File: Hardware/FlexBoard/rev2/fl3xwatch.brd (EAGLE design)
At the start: 38.4 x 17.1 mm, 23 parts, among them J1 DISP

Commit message: Rev2.1 board
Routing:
- net +3V3: track 77.7 -> 76.6 mm
- net GND: vias 4 -> 5
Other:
- board size 38.4 x 17.1 mm -> 37.4 x 17.1 mm
- board text added: "Flexible"
- board text added: "Rigid"
- board text added: "rev2.1"
- board text removed: "rev2.0"
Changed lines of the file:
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@@
 <board>
 <plain>
-<wire x1="-0.3175" y1="0" x2="38.08" y2="0" width="0" layer="20"/>
-<wire x1="38.08" y1="0" x2="38.0746" y2="17.145" width="0" layer="20"/>
-<wire x1="38.0746" y1="17.145" x2="-0.3175" y2="17.145" width="0" layer="20"/>
+<wire x1="-0.3175" y1="0" x2="37.1275" y2="0" width="0" layer="20"/>
+<wire x1="37.1275" y1="0" x2="37.1221" y2="17.145" width="0" layer="20"/>
+<wire x1="37.1221" y1="17.145" x2="-0.3175" y2="17.145" width="0" layer="20"/>
 <wire x1="-0.3175" y1="17.145" x2="-0.3175" y2="0" width="0" layer="20"/>
 <text x="12.7" y="0.9525" size="1.016" layer="25">Designed In Thailand
 By TinLethax</text>
-<text x="30.48" y="1.5875" size="1.016" layer="1">rev2.0</text>
+<text x="30.48" y="1.5875" size="1.016" layer="1">rev2.1</text>
 <text x="21.2725" y="14.605" size="1.016" layer="25" font="vector">Fl3xWatchOLED</text>
+<wire x1="13.97" y1="16.51" x2="13.97" y2="13.0175" width="0.254" layer="25"/>
+<wire x1="13.97" y1="11.7475" x2="13.97" y2="3.81" width="0.254" layer="25"/>
+<wire x1="20.32" y1="16.51" x2="20.32" y2="1.905" width="0.254" layer="25"/>
+<wire x1="20.32" y1="0.635" x2="20.32" y2="0.3175" width="0.254" layer="25"/>
+<wire x1="13.97" y1="0.635" x2="13.97" y2="0.3175" width="0.254" layer="25"/>
+<wire x1="31.115" y1="16.51" x2="31.115" y2="15.875" width="0.254" layer="25"/>
+<wire x1="31.115" y1="14.2875" x2="31.115" y2="3.175" width="0.254" layer="25"/>
+<wire x1="31.115" y1="1.27" x2="31.115" y2="0.3175" width="0.254" layer="25"/>
+<text x="15.5575" y="4.445" size="1.27" layer="25" rot="R45">Flexible</text>
+<text x="33.3375" y="14.2875" size="0.6096" layer="25" rot="R45">Flexible</text>
+<text x="2.2225" y="13.6525" size="0.6096" layer="25" rot="R45">Rigid</text>
+<text x="27.94" y="1.27" size="0.6096" layer="25" rot="R45">Rigid</text>
 </plain>
 <attributes>
@@
 <attribute name="MOUSER_PART_NUMBER" value="798-FH35C11S03SHW50" x="2.8575" y="7.62" size="1.778" layer="27" rot="R270" display="off"/>
 <attribute name="MOUSER_PRICE-STOCK" value="https://www.mouser.com/Search/Refine.aspx?Keyword=798-FH35C11S03SHW50" x="2.8575" y="7.62" size="1.778" layer="27" rot="R270" display="off"/>
-<attribute name="NAME" x="2.8575" y="3.4925" size="1.27" layer="25" rot="R270" align="center"/>
+<attribute name="NAME" x="3.81" y="11.7475" size="1.27" layer="25" rot="R270" align="center"/>
 <attribute name="VALUE" x="2.8575" y="2.54" size="1.27" layer="27" align="center"/>
 </element>
@@
 <wire x1="12.507" y1="10.16" x2="11.7475" y2="9.4005" width="0.4064" layer="1"/>
 <wire x1="11.7475" y1="9.4005" x2="11.7475" y2="8.7655" width="0.4064" layer="1"/>
-<wire x1="1.905" y1="14.185" x2="4.1275" y2="14.185" width="0.254" layer="16"/>
+<wire x1="1.905" y1="14.185" x2="2.2225" y2="14.185" width="0.254" layer="16"/>
+<wire x1="2.2225" y1="14.185" x2="4.1275" y2="14.185" width="0.254" layer="16"/>
 <wire x1="4.1275" y1="14.185" x2="4.655" y2="14.7125" width="0.254" layer="16"/>
 <wire x1="4.655" y1="14.7125" x2="10.585" y2="14.7125" width="0.254" layer="16"/>
@@
 <wire x1="4.7275" y1="7.02" x2="4.7625" y2="6.985" width="0.1524" layer="1"/>
 <wire x1="0.9885" y1="9.12" x2="1.076" y2="9.2075" width="0.1524" layer="1"/>
-<wire x1="1.076" y1="9.2075" x2="2.2225" y2="9.2075" width="0.1524" layer="1"/>
-<via x="2.2225" y="9.2075" extent="1-16" drill="0.35"/>
-<wire x1="2.2225" y1="9.2075" x2="0.635" y2="10.795" width="0.1524" layer="16"/>
-<wire x1="0.635" y1="10.795" x2="0.635" y2="13.335" width="0.1524" layer="16"/>
-<wire x1="0.635" y1="13.335" x2="1.485" y2="14.185" width="0.1524" layer="16"/>
 <wire x1="1.485" y1="14.185" x2="1.905" y2="14.185" width="0.1524" layer="16"/>
-<wire x1="2.2225" y1="9.2075" x2="0.9525" y2="9.2075" width="0.1524" layer="16"/>
 <wire x1="0.9525" y1="9.2075" x2="0.9525" y2="6.985" width="0.1524" layer="16"/>
 <wire x1="0.9525" y1="6.985" x2="4.7625" y2="6.985" width="0.1524" layer="16"/>
@@
 <wire x1="6.0325" y1="6.77" x2="9.31" y2="6.77" width="0.1524" layer="16"/>
 <wire x1="9.31" y1="6.77" x2="12.7" y2="10.16" width="0.1524" layer="16"/>
+<wire x1="0.9885" y1="9.12" x2="0.901" y2="9.2075" width="0.1524" layer="1"/>
+<wire x1="0.901" y1="9.2075" x2="0.3175" y2="9.2075" width="0.1524" layer="1"/>
+<wire x1="0.3175" y1="13.6525" x2="0.635" y2="13.97" width="0.1524" layer="1"/>
+<wire x1="0.3175" y1="13.6525" x2="0.3175" y2="9.2075" width="0.1524" layer="1"/>
+<via x="0.635" y="13.97" extent="1-16" drill="0.35"/>
+<wire x1="0.635" y1="13.97" x2="2.0075" y2="13.97" width="0.1524" layer="16"/>
+<wire x1="2.0075" y1="13.97" x2="2.2225" y2="14.185" width="0.1524" layer="16"/>
 </signal>
 <signal name="GND">
@@
 <polygon width="0.1524" layer="1">
 <vertex x="-0.3175" y="17.145"/>
-<vertex x="38.1" y="17.145"/>
-<vertex x="38.1" y="0"/>
+<vertex x="37.1475" y="17.145"/>
+<vertex x="37.1475" y="0"/>
 <vertex x="-0.3175" y="0"/>
 </polygon>
 <polygon width="0.1524" layer="16">
-<vertex x="-0.3175" y="16.8275"/>
+<vertex x="-0.3175" y="0"/>
 <vertex x="-0.3175" y="17.145"/>
-<vertex x="37.7825" y="17.145"/>
-<vertex x="38.1" y="17.145"/>
-<vertex x="38.1" y="0"/>
-<vertex x="-0.3175" y="0"/>
+<vertex x="37.1475" y="17.145"/>
+<vertex x="37.1475" y="0"/>
 </polygon>
 <wire x1="7.0875" y1="8.5725" x2="7.2799" y2="8.5725" width="0.4064" layer="1"/>
@@
 <via x="10.93490625" y="10.16" extent="1-16" drill="0.35"/>
 <wire x1="9.74" y1="8.47" x2="10.4775" y2="9.2075" width="0.254" layer="16"/>
+<via x="11.7475" y="6.6675" extent="1-16" drill="0.35"/>
 </signal>
 <signal name="N$1">
@@
 <contactref element="R4" pad="2"/>
 <contactref element="R5" pad="2"/>
-<wire x1="8.1525" y1="4.7625" x2="7.835" y2="4.7625" width="0.1524" layer="1"/>
-<wire x1="6.4875" y1="6.1675" x2="6.4875" y2="6.11" width="0.1524" layer="1"/>
-<wire x1="7.835" y1="4.7625" x2="6.4875" y2="6.11" width="0.1524" layer="1"/>
-<wire x1="7.5725" y1="2.8575" x2="8.1525" y2="3.4375" width="0.1524" layer="1"/>
-<wire x1="8.1525" y1="4.7625" x2="8.1525" y2="3.4375" width="0.1524" layer="1"/>
-<wire x1="7.5725" y1="2.8575" x2="6.35" y2="2.8575" width="0.1524" layer="1"/>
 <via x="6.35" y="2.8575" extent="1-16" drill="0.35"/>
 <wire x1="6.35" y1="2.8575" x2="7.5725" y2="2.8575" width="0.1524" layer="16"/>
+<wire x1="8.1525" y1="4.7625" x2="8.1525" y2="3.4375" width="0.254" layer="1"/>
+<wire x1="8.1525" y1="3.4375" x2="7.5725" y2="2.8575" width="0.254" layer="1"/>
+<wire x1="6.35" y1="2.8575" x2="7.5725" y2="2.8575" width="0.254" layer="1"/>
+<wire x1="6.4875" y1="6.1675" x2="7.8925" y2="4.7625" width="0.254" layer="1"/>
+<wire x1="7.8925" y1="4.7625" x2="8.1525" y2="4.7625" width="0.254" layer="1"/>
 </signal>
 <signal name="SW">
@@
 <contactref element="U$1" pad="PC1"/>
 <wire x1="6.5375" y1="11.935" x2="6.9375" y2="11.935" width="0.1524" layer="1"/>
-<wire x1="2.2225" y1="11.43" x2="2.8575" y2="11.43" width="0.1524" layer="16"/>
-<wire x1="2.8575" y1="11.43" x2="6.0325" y2="11.43" width="0.1524" layer="16"/>
+<wire x1="2.2225" y1="11.43" x2="6.0325" y2="11.43" width="0.1524" layer="16"/>
 <via x="6.0325" y="11.43" extent="1-16" drill="0.35"/>
 <wire x1="6.0325" y1="11.43" x2="6.5375" y2="11.935" width="0.1524" layer="1"/>
@@
 <wire x1="1.006" y1="7.9375" x2="1.905" y2="7.9375" width="0.1524" layer="1"/>
 <via x="1.905" y="7.9375" extent="1-16" drill="0.35"/>
-<wire x1="2.8575" y1="8.5725" x2="2.2225" y2="7.9375" width="0.1524" layer="16"/>
 <wire x1="1.905" y1="7.9375" x2="2.2225" y2="7.9375" width="0.1524" layer="16"/>
-<wire x1="2.8575" y1="8.5725" x2="2.8575" y2="11.43" width="0.1524" layer="16"/>
+<wire x1="2.2225" y1="7.9375" x2="2.2225" y2="11.43" width="0.1524" layer="16"/>
 <wire x1="1.905" y1="12.485" x2="2.2225" y2="12.1675" width="0.1524" layer="16"/>
 <wire x1="2.2225" y1="12.1675" x2="2.2225" y2="11.43" width="0.1524" layer="16"/>
@@
 <wire x1="23.366371875" y1="5.903871875" x2="23.36636875" y2="5.90386875" width="0" layer="19" extent="1-1"/>
 </signal>
-<signal name="N$3">
-<via x="21.9075" y="13.6525" extent="1-16" drill="0.35"/>
-</signal>
-<signal name="N$4">
-<via x="14.605" y="9.2075" extent="1-16" drill="0.35"/>
-</signal>
-<signal name="N$6">
-<via x="16.8275" y="7.9375" extent="1-16" drill="0.35"/>
-</signal>
-<signal name="N$8">
-<via x="14.605" y="5.715" extent="1-16" drill="0.35"/>
-</signal>
-<signal name="N$9">
-<via x="16.8275" y="4.7625" extent="1-16" drill="0.35"/>
-</signal>
-<signal name="N$10">
-<via x="34.925" y="14.605" extent="1-16" drill="0.35"/>
-</signal>
-<signal name="N$11">
-<via x="30.48" y="13.335" extent="1-16" drill="0.35"/>
-</signal>
-<signal name="N$12">
-<via x="31.4325" y="5.3975" extent="1-16" drill="0.35"/>
-</signal>
-<signal name="N$13">
-<via x="26.3525" y="1.5875" extent="1-16" drill="0.35"/>
-</signal>
-<signal name="N$14">
-<via x="21.9075" y="1.5875" extent="1-16" drill="0.35"/>
-</signal>
-<signal name="N$15">
-<via x="35.8775" y="4.1275" extent="1-16" drill="0.35"/>
-</signal>
-<signal name="N$16">
-<via x="20.0025" y="15.24" extent="1-16" drill="0.35"/>
-</signal>
 </signals>

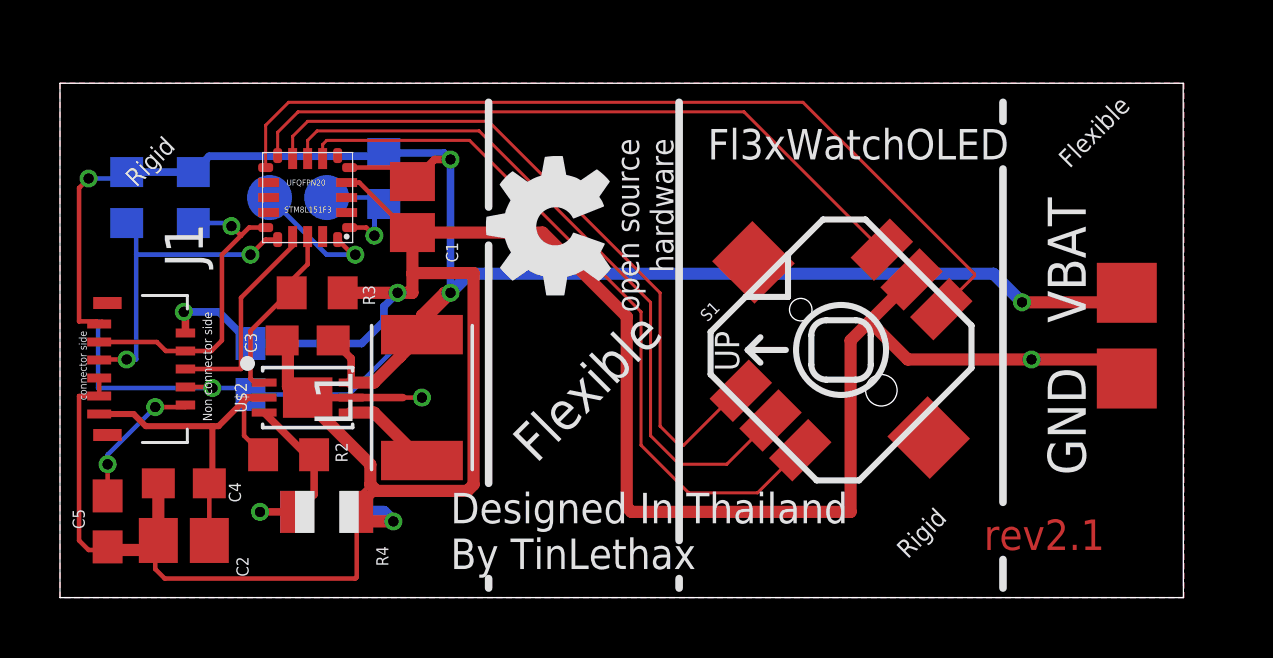
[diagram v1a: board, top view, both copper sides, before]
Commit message: added Rev 2.2 PCB
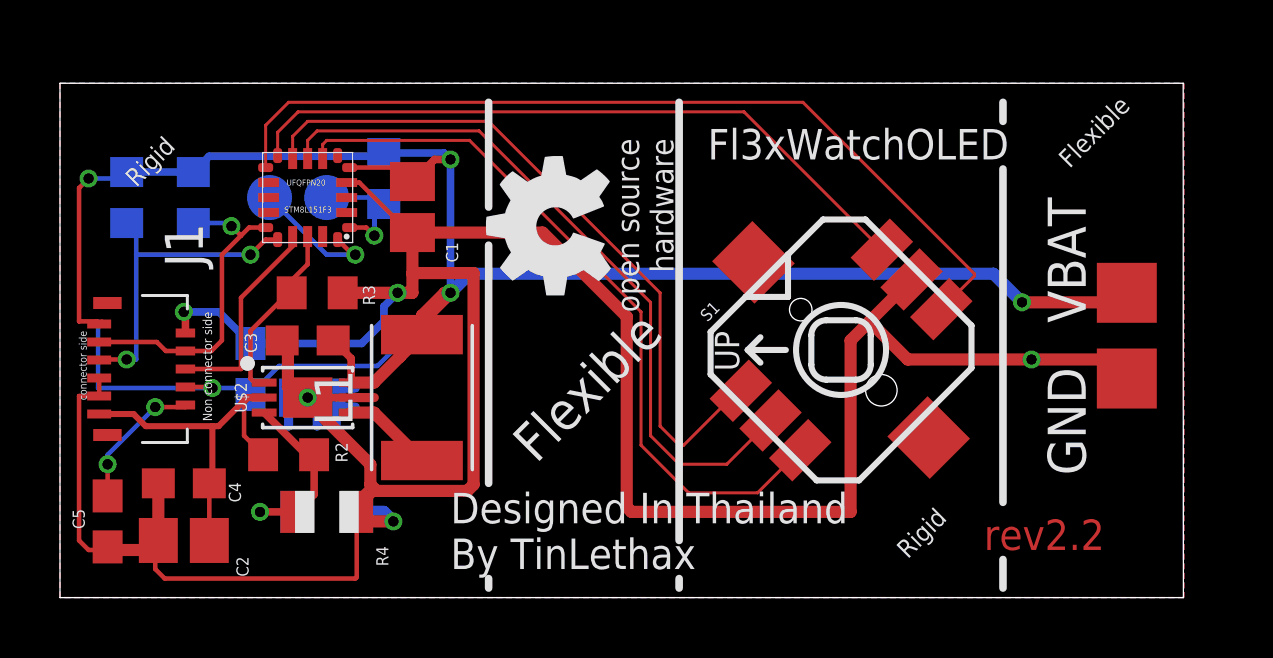
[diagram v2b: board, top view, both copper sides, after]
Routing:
- net GND: track 110.8 -> 108.6 mm
- net N$5: track 0.00 -> 0.63 mm
- net N$4: track 0.00 -> 0.63 mm
- net N$3: track 0.00 -> 0.63 mm
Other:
- board text added: "rev2.2"
- board text removed: "rev2.1"
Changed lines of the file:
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@@
 <drawing>
 <settings>
-<setting alwaysvectorfont="yes"/>
+<setting alwaysvectorfont="no"/>
 <setting verticaltext="up"/>
 </settings>
@@
 <text x="12.7" y="0.9525" size="1.016" layer="25">Designed In Thailand
 By TinLethax</text>
-<text x="30.48" y="1.5875" size="1.016" layer="1">rev2.1</text>
+<text x="30.48" y="1.5875" size="1.016" layer="1">rev2.2</text>
 <text x="21.2725" y="14.605" size="1.016" layer="25" font="vector">Fl3xWatchOLED</text>
 <wire x1="13.97" y1="16.51" x2="13.97" y2="13.0175" width="0.254" layer="25"/>
@@
 <text x="2.2225" y="13.6525" size="0.6096" layer="25" rot="R45">Rigid</text>
 <text x="27.94" y="1.27" size="0.6096" layer="25" rot="R45">Rigid</text>
+<rectangle x1="6.985" y1="6.0325" x2="9.2075" y2="7.3025" layer="16"/>
 </plain>
 <attributes>
@@
 <classes>
 <class number="0" name="default" width="0" drill="0">
+</class>
+<class number="1" name="Ground" width="0" drill="0">
 </class>
 </classes>
@@
 <wire x1="12.485" y1="14.82" x2="12.7" y2="14.605" width="0.254" layer="16"/>
 <wire x1="12.7" y1="14.605" x2="12.7" y2="10.16" width="0.254" layer="16"/>
-<wire x1="6.0325" y1="6.77" x2="9.31" y2="6.77" width="0.1524" layer="16"/>
-<wire x1="9.31" y1="6.77" x2="12.7" y2="10.16" width="0.1524" layer="16"/>
+<wire x1="6.0325" y1="6.77" x2="6.985" y2="7.7225" width="0.1524" layer="16"/>
+<wire x1="10.2625" y1="7.7225" x2="6.985" y2="7.7225" width="0.1524" layer="16"/>
+<wire x1="10.2625" y1="7.7225" x2="12.7" y2="10.16" width="0.1524" layer="16"/>
 <wire x1="0.9885" y1="9.12" x2="0.901" y2="9.2075" width="0.1524" layer="1"/>
 <wire x1="0.901" y1="9.2075" x2="0.3175" y2="9.2075" width="0.1524" layer="1"/>
@@
 <contactref element="GND" pad="TP"/>
 <contactref element="S1" pad="GND"/>
-<wire x1="7.9375" y1="6.6675" x2="9.3875" y2="6.6675" width="0.254" layer="1"/>
+<wire x1="7.9375" y1="6.6675" x2="8.89" y2="6.6675" width="0.254" layer="1"/>
+<wire x1="8.89" y1="6.6675" x2="9.3875" y2="6.6675" width="0.254" layer="1"/>
 <wire x1="7.405" y1="8.5725" x2="7.405" y2="7.2" width="0.1524" layer="1"/>
 <wire x1="7.405" y1="7.2" x2="7.9375" y2="6.6675" width="0.1524" layer="1"/>
@@
 <wire x1="2.8575" y1="0.9525" x2="2.8575" y2="1.8025" width="0.1524" layer="1"/>
 <wire x1="2.8575" y1="1.8025" x2="2.96" y2="1.905" width="0.1524" layer="1"/>
-<wire x1="10.4775" y1="6.6675" x2="11.1125" y2="6.6675" width="0.1524" layer="1"/>
-<wire x1="11.1125" y1="6.6675" x2="11.7475" y2="6.6675" width="0.1524" layer="1"/>
 <wire x1="10.93490625" y1="10.16" x2="11.43" y2="10.16" width="0.4064" layer="1"/>
 <wire x1="11.43" y1="10.16" x2="11.43" y2="10.795" width="0.4064" layer="1"/>
@@
 <wire x1="10.795" y1="2.54" x2="10.4775" y2="2.8575" width="0.4064" layer="16"/>
 <via x="32.0675" y="7.9375" extent="1-16" drill="0.35"/>
-<polygon width="0.1524" layer="1">
-<vertex x="-0.3175" y="17.145"/>
-<vertex x="37.1475" y="17.145"/>
-<vertex x="37.1475" y="0"/>
-<vertex x="-0.3175" y="0"/>
-</polygon>
-<polygon width="0.1524" layer="16">
-<vertex x="-0.3175" y="0"/>
-<vertex x="-0.3175" y="17.145"/>
-<vertex x="37.1475" y="17.145"/>
-<vertex x="37.1475" y="0"/>
-</polygon>
 <wire x1="7.0875" y1="8.5725" x2="7.2799" y2="8.5725" width="0.4064" layer="1"/>
 <wire x1="7.2799" y1="8.5725" x2="7.2799" y2="7.0301125" width="0.4064" layer="1"/>
@@
 <wire x1="9.5725" y1="2.8575" x2="9.5725" y2="3.31020625" width="0.1524" layer="1"/>
 <wire x1="9.5725" y1="3.31020625" x2="10.02735" y2="3.76505625" width="0.1524" layer="1"/>
-<wire x1="9.3875" y1="6.6675" x2="11.1125" y2="6.6675" width="0.254" layer="1"/>
 <wire x1="0.9885" y1="6.72" x2="0.3175" y2="6.72" width="0.1524" layer="1"/>
 <wire x1="0.3175" y1="6.72" x2="0.3175" y2="1.905" width="0.1524" layer="1"/>
@@
 <via x="10.93490625" y="10.16" extent="1-16" drill="0.35"/>
 <wire x1="9.74" y1="8.47" x2="10.4775" y2="9.2075" width="0.254" layer="16"/>
-<via x="11.7475" y="6.6675" extent="1-16" drill="0.35"/>
+<polygon width="0.1524" layer="1" spacing="0.8128" pour="hatch">
+<vertex x="-0.3175" y="17.145"/>
+<vertex x="37.1475" y="17.145"/>
+<vertex x="37.1475" y="0"/>
+<vertex x="-0.3175" y="0"/>
+</polygon>
+<polygon width="0.1524" layer="16" spacing="0.8128" pour="hatch">
+<vertex x="-0.3175" y="17.145"/>
+<vertex x="37.1475" y="17.145"/>
+<vertex x="37.1475" y="0"/>
+<vertex x="-0.3175" y="0"/>
+</polygon>
+<via x="7.9375" y="6.6675" extent="1-16" drill="0.35"/>
+<wire x1="9.3875" y1="6.6675" x2="10.16" y2="6.6675" width="0.3048" layer="1"/>
 </signal>
 <signal name="N$1">
@@
 <wire x1="23.366371875" y1="5.903871875" x2="23.36636875" y2="5.90386875" width="0" layer="19" extent="1-1"/>
 </signal>
+<signal name="N$3">
+<wire x1="8.89" y1="6.985" x2="9.525" y2="6.985" width="0.3048" layer="16"/>
+</signal>
+<signal name="N$4">
+<wire x1="8.89" y1="6.35" x2="9.525" y2="6.35" width="0.3048" layer="16"/>
+</signal>
+<signal name="N$5">
+<wire x1="7.3025" y1="6.35" x2="7.3025" y2="5.715" width="0.3048" layer="16"/>
+</signal>
+<signal name="N$6">
+<wire x1="8.255" y1="6.0325" x2="8.255" y2="5.715" width="0.3048" layer="16"/>
+</signal>
+<signal name="N$8">
+<wire x1="8.89" y1="6.0325" x2="8.89" y2="5.715" width="0.3048" layer="16"/>
+</signal>
 </signals>
